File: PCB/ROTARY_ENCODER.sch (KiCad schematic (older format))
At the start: 4 parts

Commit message: Annotated Schematic
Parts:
- gave numbers to parts that had none: 4
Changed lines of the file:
@@
 $EndDescr
 $Comp
-L Device:Rotary_Encoder_Switch SW?
+L Device:Rotary_Encoder_Switch SW4
 U 1 1 5E8BF4A3
 P 5800 4050
-F 0 "SW?" H 5800 4417 50  0000 C CNN
+F 0 "SW4" H 5800 4417 50  0000 C CNN
 F 1 "ENCODER" H 5800 4326 50  0000 C CNN
 F 2 "" H 5650 4210 50  0001 C CNN
-F 3 "~" H 5800 4310 50  0001 C CNN
+F 3 "" H 5800 4310 50  0001 C CNN
 	1    5800 4050
 	1    0    0    -1
 $EndComp
 $Comp
-L Device:R_Small R?
+L Device:R_Small R25
 U 1 1 5E8BFE00
 P 5250 3800
-F 0 "R?" H 5309 3754 50  0000 L CNN
+F 0 "R25" H 5309 3754 50  0000 L CNN
 F 1 "10k" H 5309 3845 50  0000 L CNN
 F 2 "" H 5250 3800 50  0001 C CNN
-F 3 "~" H 5250 3800 50  0001 C CNN
+F 3 "" H 5250 3800 50  0001 C CNN
 	1    5250 3800
 	-1   0    0    1
 $EndComp
 $Comp
-L Device:R_Small R?
+L Device:R_Small R26
 U 1 1 5E8C002C
 P 5250 4300
-F 0 "R?" H 5309 4254 50  0000 L CNN
+F 0 "R26" H 5309 4254 50  0000 L CNN
 F 1 "10k" H 5309 4345 50  0000 L CNN
 F 2 "" H 5250 4300 50  0001 C CNN
-F 3 "~" H 5250 4300 50  0001 C CNN
+F 3 "" H 5250 4300 50  0001 C CNN
 	1    5250 4300
 	-1   0    0    1
@@
 	5250 3950 5250 3900
 $Comp
-L power:+3.3V #PWR?
+L power:+3.3V #PWR0126
 U 1 1 5E8C03DD
 P 5250 3650
-F 0 "#PWR?" H 5250 3500 50  0001 C CNN
+F 0 "#PWR0126" H 5250 3500 50  0001 C CNN
 F 1 "+3.3V" H 5265 3823 50  0000 C CNN
 F 2 "" H 5250 3650 50  0001 C CNN
@@
 B
 $Comp
-L power:GND #PWR?
+L power:GND #PWR0128
 U 1 1 5E8C2AF2
 P 5450 4050
-F 0 "#PWR?" H 5450 3800 50  0001 C CNN
+F 0 "#PWR0128" H 5450 3800 50  0001 C CNN
 F 1 "GND" V 5455 3922 50  0000 R CNN
 F 2 "" H 5450 4050 50  0001 C CNN
@@
 	5250 4150 5500 4150
 $Comp
-L power:+3.3V #PWR?
+L power:+3.3V #PWR0127
 U 1 1 5E8C4253
 P 5250 4450
-F 0 "#PWR?" H 5250 4300 50  0001 C CNN
+F 0 "#PWR0127" H 5250 4300 50  0001 C CNN
 F 1 "+3.3V" H 5265 4623 50  0000 C CNN
 F 2 "" H 5250 4450 50  0001 C CNN
@@
 Connection ~ 5250 4150
 $Comp
-L Device:R_Small R?
+L Device:R_Small R27
 U 1 1 5E8C58DC
 P 6150 3800
-F 0 "R?" H 6091 3754 50  0000 R CNN
+F 0 "R27" H 6091 3754 50  0000 R CNN
 F 1 "10k" H 6091 3845 50  0000 R CNN
 F 2 "" H 6150 3800 50  0001 C CNN
-F 3 "~" H 6150 3800 50  0001 C CNN
+F 3 "" H 6150 3800 50  0001 C CNN
 	1    6150 3800
 	-1   0    0    1
@@
 	6150 3950 6150 3900
 $Comp
-L power:+3.3V #PWR?
+L power:+3.3V #PWR0129
 U 1 1 5E8C5D26
 P 6150 3650
-F 0 "#PWR?" H 6150 3500 50  0001 C CNN
+F 0 "#PWR0129" H 6150 3500 50  0001 C CNN
 F 1 "+3.3V" H 6165 3823 50  0000 C CNN
 F 2 "" H 6150 3650 50  0001 C CNN
@@
 	6150 3650 6150 3700
 $Comp
-L power:GND #PWR?
+L power:GND #PWR0130
 U 1 1 5E8C6704
 P 6150 4200
-F 0 "#PWR?" H 6150 3950 50  0001 C CNN
+F 0 "#PWR0130" H 6150 3950 50  0001 C CNN
 F 1 "GND" H 6155 4027 50  0000 C CNN
 F 2 "" H 6150 4200 50  0001 C CNN

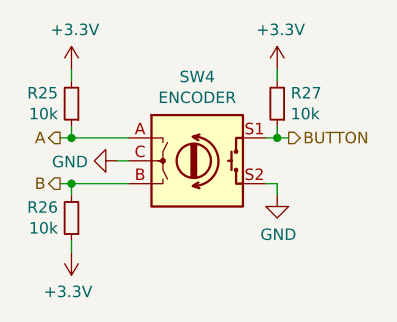
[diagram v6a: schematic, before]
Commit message: Increased VCC from 3v3 to 5v
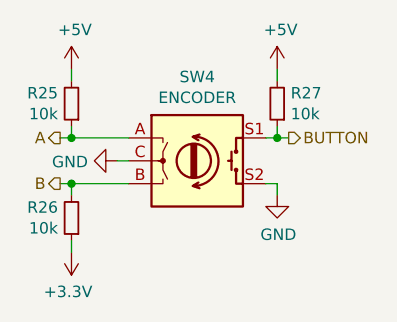
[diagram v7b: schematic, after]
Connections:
- net +3V3: no longer R25.2, R27.2
- new net +5V: R25.2, R27.2
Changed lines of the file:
@@
 $Descr A4 11693 8268
 encoding utf-8
-Sheet 19 25
+Sheet 18 25
 Title ""
 Date ""
@@
 Wire Wire Line
 	5250 3950 5250 3900
-$Comp
-L power:+3.3V #PWR0126
-U 1 1 5E8C03DD
-P 5250 3650
-F 0 "#PWR0126" H 5250 3500 50  0001 C CNN
-F 1 "+3.3V" H 5265 3823 50  0000 C CNN
-F 2 "" H 5250 3650 50  0001 C CNN
-F 3 "" H 5250 3650 50  0001 C CNN
-	1    5250 3650
-	1    0    0    -1
-$EndComp
 Wire Wire Line
 	5250 3650 5250 3700
@@
 Wire Wire Line
 	6150 3950 6150 3900
-$Comp
-L power:+3.3V #PWR0129
-U 1 1 5E8C5D26
-P 6150 3650
-F 0 "#PWR0129" H 6150 3500 50  0001 C CNN
-F 1 "+3.3V" H 6165 3823 50  0000 C CNN
-F 2 "" H 6150 3650 50  0001 C CNN
-F 3 "" H 6150 3650 50  0001 C CNN
-	1    6150 3650
-	1    0    0    -1
-$EndComp
 Wire Wire Line
 	6150 3650 6150 3700
@@
 	6200 3950 6150 3950
 Connection ~ 6150 3950
+$Comp
+L power:+5V #PWR?
+U 1 1 5E91E86F
+P 6150 3650
+AR Path="/5E8A6686/5E91E86F" Ref="#PWR?"  Part="1"
+AR Path="/5E8BEE14/5E91E86F" Ref="#PWR?"  Part="1"
+F 0 "#PWR?" H 6150 3500 50  0001 C CNN
+F 1 "+5V" H 6165 3823 50  0000 C CNN
+F 2 "" H 6150 3650 50  0001 C CNN
+F 3 "" H 6150 3650 50  0001 C CNN
+	1    6150 3650
+	1    0    0    -1
+$EndComp
+$Comp
+L power:+5V #PWR?
+U 1 1 5E91E997
+P 5250 3650
+AR Path="/5E8A6686/5E91E997" Ref="#PWR?"  Part="1"
+AR Path="/5E8BEE14/5E91E997" Ref="#PWR?"  Part="1"
+F 0 "#PWR?" H 5250 3500 50  0001 C CNN
+F 1 "+5V" H 5265 3823 50  0000 C CNN
+F 2 "" H 5250 3650 50  0001 C CNN
+F 3 "" H 5250 3650 50  0001 C CNN
+	1    5250 3650
+	1    0    0    -1
+$EndComp
 $EndSCHEMATC

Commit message: Added Humidity and temperature sensors
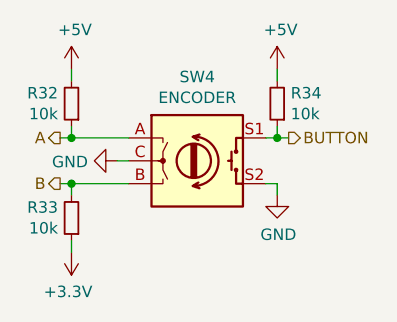
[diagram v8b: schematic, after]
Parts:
- renumbered R25 to R32, R26 to R33, R27 to R34
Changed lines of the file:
@@
 $EndComp
 $Comp
-L Device:R_Small R25
+L Device:R_Small R32
 U 1 1 5E8BFE00
 P 5250 3800
-F 0 "R25" H 5309 3754 50  0000 L CNN
+F 0 "R32" H 5309 3754 50  0000 L CNN
 F 1 "10k" H 5309 3845 50  0000 L CNN
 F 2 "" H 5250 3800 50  0001 C CNN
@@
 $EndComp
 $Comp
-L Device:R_Small R26
+L Device:R_Small R33
 U 1 1 5E8C002C
 P 5250 4300
-F 0 "R26" H 5309 4254 50  0000 L CNN
+F 0 "R33" H 5309 4254 50  0000 L CNN
 F 1 "10k" H 5309 4345 50  0000 L CNN
 F 2 "" H 5250 4300 50  0001 C CNN
@@
 B
 $Comp
-L power:GND #PWR0128
+L power:GND #PWR0131
 U 1 1 5E8C2AF2
 P 5450 4050
-F 0 "#PWR0128" H 5450 3800 50  0001 C CNN
+F 0 "#PWR0131" H 5450 3800 50  0001 C CNN
 F 1 "GND" V 5455 3922 50  0000 R CNN
 F 2 "" H 5450 4050 50  0001 C CNN
@@
 	5250 4150 5500 4150
 $Comp
-L power:+3.3V #PWR0127
+L power:+3.3V #PWR0130
 U 1 1 5E8C4253
 P 5250 4450
-F 0 "#PWR0127" H 5250 4300 50  0001 C CNN
+F 0 "#PWR0130" H 5250 4300 50  0001 C CNN
 F 1 "+3.3V" H 5265 4623 50  0000 C CNN
 F 2 "" H 5250 4450 50  0001 C CNN
@@
 Connection ~ 5250 4150
 $Comp
-L Device:R_Small R27
+L Device:R_Small R34
 U 1 1 5E8C58DC
 P 6150 3800
-F 0 "R27" H 6091 3754 50  0000 R CNN
+F 0 "R34" H 6091 3754 50  0000 R CNN
 F 1 "10k" H 6091 3845 50  0000 R CNN
 F 2 "" H 6150 3800 50  0001 C CNN
@@
 	6150 3650 6150 3700
 $Comp
-L power:GND #PWR0130
+L power:GND #PWR0133
 U 1 1 5E8C6704
 P 6150 4200
-F 0 "#PWR0130" H 6150 3950 50  0001 C CNN
+F 0 "#PWR0133" H 6150 3950 50  0001 C CNN
 F 1 "GND" H 6155 4027 50  0000 C CNN
 F 2 "" H 6150 4200 50  0001 C CNN
@@
 P 6150 3650
 AR Path="/5E8A6686/5E91E86F" Ref="#PWR?"  Part="1"
-AR Path="/5E8BEE14/5E91E86F" Ref="#PWR?"  Part="1"
-F 0 "#PWR?" H 6150 3500 50  0001 C CNN
+AR Path="/5E8BEE14/5E91E86F" Ref="#PWR0132"  Part="1"
+F 0 "#PWR0132" H 6150 3500 50  0001 C CNN
 F 1 "+5V" H 6165 3823 50  0000 C CNN
 F 2 "" H 6150 3650 50  0001 C CNN
@@
 P 5250 3650
 AR Path="/5E8A6686/5E91E997" Ref="#PWR?"  Part="1"
-AR Path="/5E8BEE14/5E91E997" Ref="#PWR?"  Part="1"
-F 0 "#PWR?" H 5250 3500 50  0001 C CNN
+AR Path="/5E8BEE14/5E91E997" Ref="#PWR0129"  Part="1"
+F 0 "#PWR0129" H 5250 3500 50  0001 C CNN
 F 1 "+5V" H 5265 3823 50  0000 C CNN
 F 2 "" H 5250 3650 50  0001 C CNN
